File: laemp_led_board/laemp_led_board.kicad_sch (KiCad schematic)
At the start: 90 parts

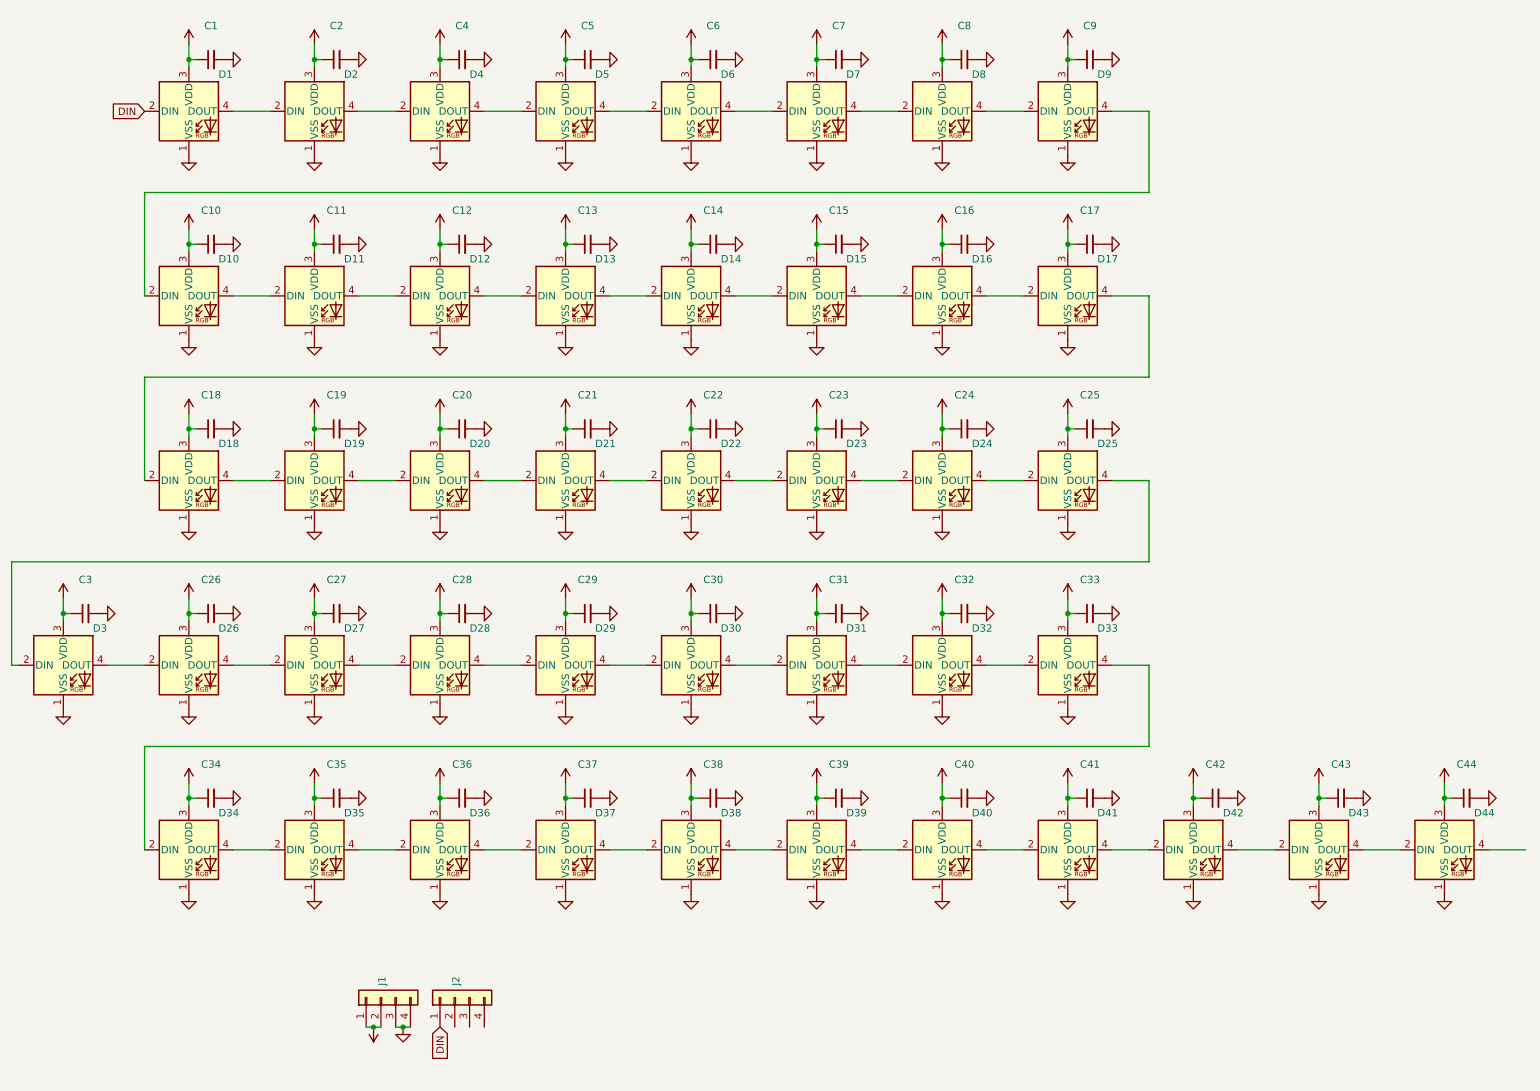
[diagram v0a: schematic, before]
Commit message: renamed led board
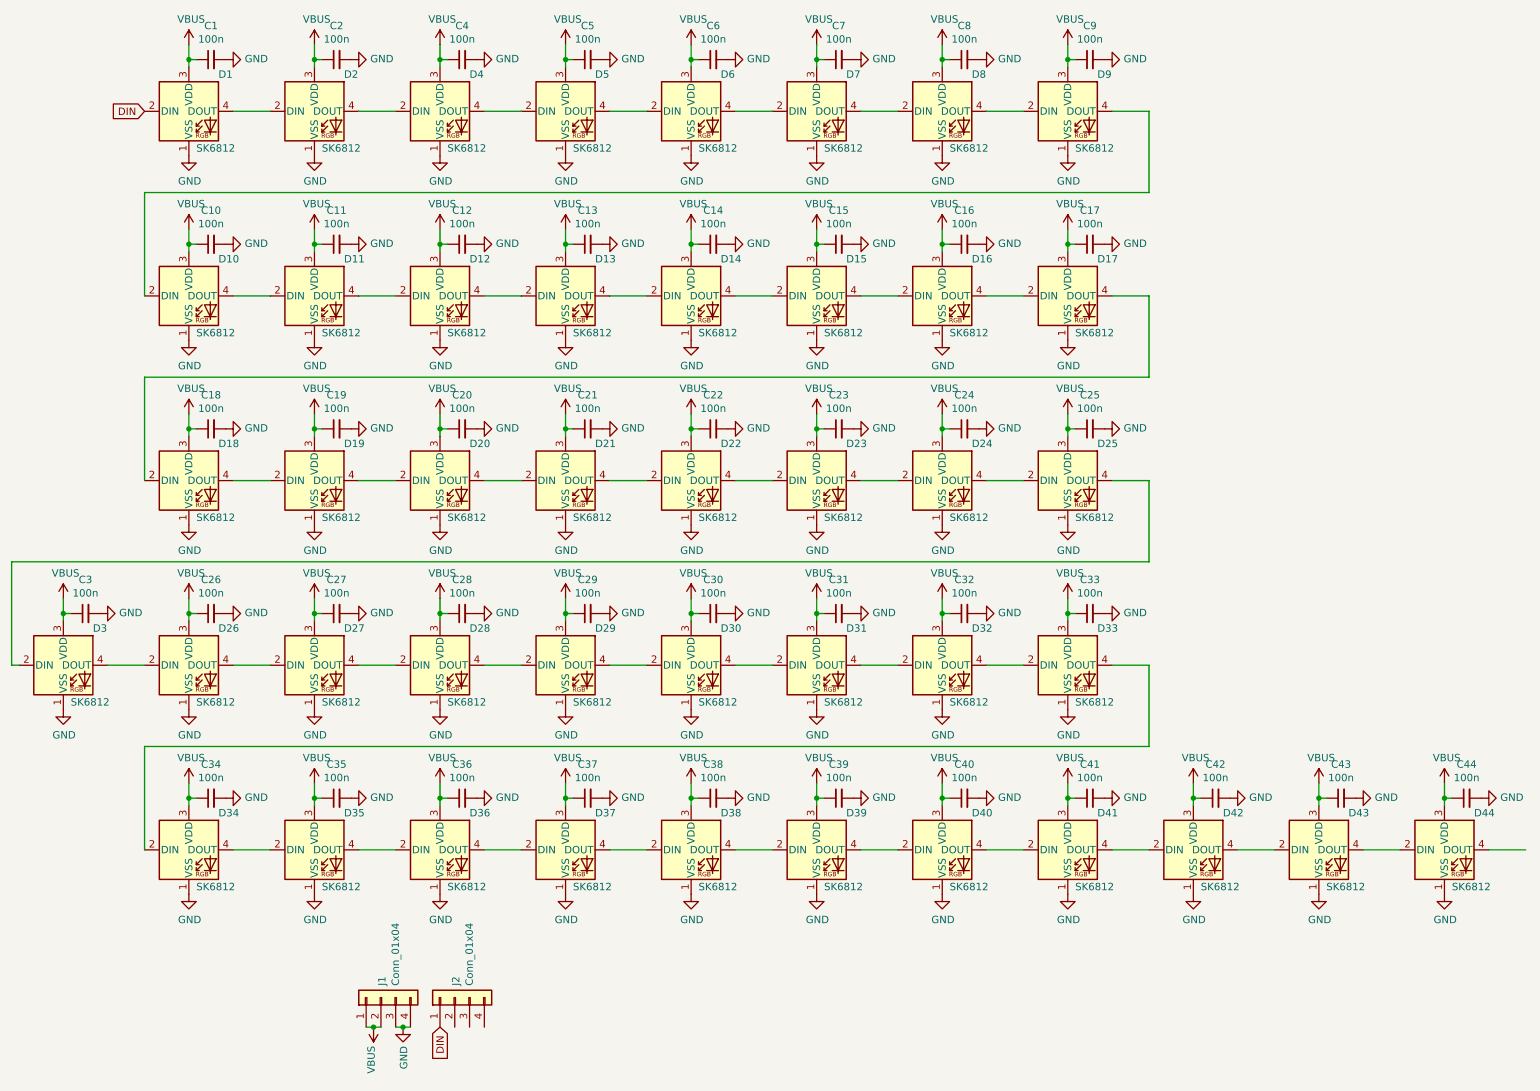
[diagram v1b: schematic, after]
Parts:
- C1, C10, C11, C12, C13, C14, C15, C16, C17, C18, C19, C2, C20, C21, C22, C23, C24, C25, C26, C27, C28, C29, C3, C30, C31, C32, C33, C34, C35, C36, C37, C38, C39, C4, C40, C41, C42, C43, C44, C5, C6, C7, C8, C9: value (none) -> 100n; footprint (none) -> otter:C_0402
- D1, D10, D11, D12, D13, D14, D15, D16, D17, D18, D19, D2, D20, D21, D22, D23, D24, D25, D26, D27, D28, D29, D3, D30, D31, D32, D33, D34, D35, D36, D37, D38, D39, D4, D40, D41, D42, D43, D44, D5, D6, D7, D8, D9: value (none) -> SK6812; footprint (none) -> LED_SMD:LED_SK6812_PLCC4_5.0x5.0mm_P3.2mm
- J1, J2: value (none) -> Conn_01x04; footprint (none) -> Connector_PinHeader_2.54mm:PinHeader_1x04_P2.54mm_Vertical_SMD_Pin1Left
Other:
- company: (none) -> Jana Marie Hemsing
- title: (none) -> LÄMP LED Board
